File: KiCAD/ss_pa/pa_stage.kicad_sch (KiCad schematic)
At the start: 0 parts

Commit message: KiCad revC: ss_pa pa_stage initial draft + protoshield additions
ss_pa:
- First pass on pa_stage.kicad_sch: Q1/Q2 push-pull FETs, T1 output
  transformer, T2 drain-feed transformer, C3 drain snubber,
  per-FET source sense (2x 0.22R parallel per FET = 0.11R to GND)
  with Source_Sense_A/B taps, J1 coax output
- Known pending (per user): bias network, input DC-block caps,
  drain-gate feedback networks, +13.8V bulk electrolytic
- Known issues flagged in review (to be fixed on next edit):
  Q1/Q2 are IRF540N (should be IRF510 — gate capacitance mismatch),
  T2 phasing (both corresponding ends at CT → parallel winding
  instead of push-pull), no RFC between +13.8V and T2 CT
- First netlist export captured (ss_pa.net)

protoshield:
- Added capacitors C2-C3, resistors R1-R2, power symbols
  (#PWR5, #PWR22-24)

Co-Authored-By: Claude Opus 4.7 <noreply@anthropic.com>
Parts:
- added C1, C2: 1uF, symbol Device:C
- added C3: 33pF, symbol Device:C
- added J1: Conn_Coaxial_Small, symbol Connector:Conn_Coaxial_Small
- added Q1, Q2: IRF540N, Package_TO_SOT_THT:TO-220-3_Vertical, symbol Transistor_FET:IRF540N
- added R1, R2, R3, R4: 0.22R, symbol Device:R_US
- added T1, T2: Transformer_1P_1S, symbol Device:Transformer_1P_1S
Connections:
- new net: C3.2, Q2.2 (D), T1.2 (AB), T2.2 (AB)
- new net: J1.1 (In), T1.4 (SB)
- new net: C3.1, Q1.2 (D), T1.1 (AA), T2.4 (SB)
- new net +13.8V: C1.1, C2.2, T2.1 (AA), T2.3 (SA)
- new net GND: C1.2, C2.1, J1.2 (Ext), R1.2, R2.2, R3.1, R4.1, T1.3 (SA)
- new net Source_Sense_A: Q1.3 (S), R1.1, R2.1
- new net Source_Sense_B: Q2.3 (S), R3.2, R4.2
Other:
- note added: "Pin 2 and pin 3 = phase (dot)"

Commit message: KiCad revC: add xmitter:IRF510 symbol, fix Q1/Q2 metadata on pa_stage
- Added IRF510 TO-220 symbol to shared xmitter.kicad_sym (cloned IRF540N
  body graphic since pinout is identical: G=pin1, D=pin2+tab, S=pin3).
  Vishay datasheet URL, 5.6A/100V description, MPN IRF510PBF. KiCad
  standard libs don't ship an IRF510 symbol, so hosting it in the
  project's shared library.
- Updated Q1/Q2 instance-level Datasheet and Description on pa_stage
  to match (Value field was already IRF510). User will swap lib_id
  from Transistor_FET:IRF540N to xmitter:IRF510 via Change Symbol in
  KiCad to clear the lib_symbol_mismatch ERC warning.

Co-Authored-By: Claude Opus 4.7 <noreply@anthropic.com>
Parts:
- removed Q1, Q2: IRF540N, Package_TO_SOT_THT:TO-220-3_Vertical, symbol Transistor_FET:IRF540N
- added Q3, Q4: IRF510, Package_TO_SOT_THT:TO-220-3_Vertical, symbol xmitter:IRF510
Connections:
- net Source_Sense_A: now also Q3.3 (S)
- net Source_Sense_B: now also Q4.3 (S)
- net at C3.2, T1.2 (AB), T2.2 (AB): now also Q4.2 (D)
- net at C3.1, T1.1 (AA), T2.4 (SB): now also Q3.2 (D)
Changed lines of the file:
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@@
-	)
-	(symbol
-		(lib_id "Transistor_FET:IRF540N")
-		(at 158.75 109.22 0)
-		(mirror x)
-		(unit 1)
-		(body_style 1)
-		(exclude_from_sim no)
-		(in_bom yes)
-		(on_board yes)
-		(in_pos_files yes)
-		(dnp no)
-		(property "Reference" "Q2"
-			(at 165.1 107.9499 0)
-			(show_name no)
-			(do_not_autoplace no)
-			(effects
-				(font
-					(size 1.27 1.27)
-				)
-				(justify left)
-			)
-		)
-		(property "Value" "IRF540N"
-			(at 165.1 110.4899 0)
-			(show_name no)
-			(do_not_autoplace no)
-			(effects
-				(font
-					(size 1.27 1.27)
-				)
-				(justify left)
-			)
-		)
-		(property "Footprint" "Package_TO_SOT_THT:TO-220-3_Vertical"
-			(at 163.83 107.315 0)
-			(hide yes)
-			(show_name no)
-			(do_not_autoplace no)
-			(effects
-				(font
-					(size 1.27 1.27)
-					(italic yes)
-				)
-				(justify left)
-			)
-		)
-		(property "Datasheet" "http://www.irf.com/product-info/datasheets/data/irf540n.pdf"
-			(at 163.83 105.41 0)
-			(hide yes)
-			(show_name no)
-			(do_not_autoplace no)
-			(effects
-				(font
-					(size 1.27 1.27)
-				)
-				(justify left)
-			)
-		)
-		(property "Description" "33A Id, 100V Vds, HEXFET N-Channel MOSFET, TO-220"
-			(at 158.75 109.22 0)
-			(hide yes)
-			(show_name no)
-			(do_not_autoplace no)
-			(effects
-				(font
-					(size 1.27 1.27)
-				)
-			)
-		)
-		(pin "2"
-		)
-		(pin "3"
-		)
-		(pin "1"
-		)
-		(instances
-			(project "ss_pa"
-				(path "/7b9fe991-54d6-43c4-a637-0ed9ee982c42/6995ca2b-35a4-4871-8cf2-3a0067e62105"
-					(reference "Q2")
-					(unit 1)
-				)
-			)
-		)
 	)
 	(symbol
@@
 	)
 	(symbol
-		(lib_id "Transistor_FET:IRF540N")
+		(lib_id "xmitter:IRF510")
 		(at 158.75 74.93 0)
 		(unit 1)
@@
 		(dnp no)
 		(fields_autoplaced yes)
-		(property "Reference" "Q1"
+		(property "Reference" "Q3"
 			(at 165.1 73.6599 0)
 			(show_name no)
@@
 			)
 		)
-		(property "Value" "IRF540N"
+		(property "Value" "IRF510"
 			(at 165.1 76.1999 0)
 			(show_name no)
@@
 			)
 		)
-		(property "Datasheet" "http://www.irf.com/product-info/datasheets/data/irf540n.pdf"
+		(property "Datasheet" "https://www.vishay.com/docs/91015/sihf510.pdf"
 			(at 163.83 78.74 0)
 			(hide yes)
@@
 			)
 		)
-		(property "Description" "33A Id, 100V Vds, HEXFET N-Channel MOSFET, TO-220"
+		(property "Description" "5.6A Id, 100V Vds, HEXFET N-Channel MOSFET, TO-220"
 			(at 158.75 74.93 0)
 			(hide yes)
@@
 			)
 		)
-		(pin "1"
+		(property "Manufacturer" "Vishay"
+			(at 158.75 74.93 0)
+			(hide yes)
+			(show_name no)
+			(do_not_autoplace no)
+			(effects
+				(font
+					(size 1.27 1.27)
+				)
+			)
+		)
+		(property "MPN" "IRF510PBF"
+			(at 158.75 74.93 0)
+			(hide yes)
+			(show_name no)
+			(do_not_autoplace no)
+			(effects
+				(font
+					(size 1.27 1.27)
+				)
+			)
 		)
 		(pin "2"
 		)
+		(pin "1"
+		)
 		(pin "3"
 		)
@@
 			(project "ss_pa"
 				(path "/7b9fe991-54d6-43c4-a637-0ed9ee982c42/6995ca2b-35a4-4871-8cf2-3a0067e62105"
-					(reference "Q1")
+					(reference "Q3")
 					(unit 1)
 				)
@@
 					(unit 1)
 				)
+			)
+		)
+	)
+	(symbol
+		(lib_id "xmitter:IRF510")
+		(at 158.75 109.22 0)
+		(mirror x)
+		(unit 1)
+		(body_style 1)
+		(exclude_from_sim no)
+		(in_bom yes)
+		(on_board yes)
+		(in_pos_files yes)
+		(dnp no)
+		(property "Reference" "Q4"
+			(at 165.1 110.4901 0)
+			(show_name no)
+			(do_not_autoplace no)
+			(effects
+				(font
+					(size 1.27 1.27)
+				)
+				(justify left)
+			)
+		)
+		(property "Value" "IRF510"
+			(at 165.1 107.9501 0)
+			(show_name no)
+			(do_not_autoplace no)
+			(effects
+				(font
+					(size 1.27 1.27)
+				)
+				(justify left)
+			)
+		)
+		(property "Footprint" "Package_TO_SOT_THT:TO-220-3_Vertical"
+			(at 163.83 107.315 0)
+			(hide yes)
+			(show_name no)
+			(do_not_autoplace no)
+			(effects
+				(font
+					(size 1.27 1.27)
+					(italic yes)
+				)
+				(justify left)
+			)
+		)
+		(property "Datasheet" "https://www.vishay.com/docs/91015/sihf510.pdf"
+			(at 163.83 105.41 0)
+			(hide yes)
+			(show_name no)
+			(do_not_autoplace no)
+			(effects
+				(font
+					(size 1.27 1.27)
+				)
+				(justify left)
+			)
+		)
+		(property "Description" "5.6A Id, 100V Vds, HEXFET N-Channel MOSFET, TO-220"
+			(at 158.75 109.22 0)
+			(hide yes)
+			(show_name no)
+			(do_not_autoplace no)
+			(effects
+				(font
+					(size 1.27 1.27)
+				)
+			)
+		)
+		(property "Manufacturer" "Vishay"
+			(at 158.75 109.22 0)
+			(hide yes)
+			(show_name no)
+			(do_not_autoplace no)
+			(effects
+				(font
+					(size 1.27 1.27)
+				)
+			)
+		)
+		(property "MPN" "IRF510PBF"
+			(at 158.75 109.22 0)
+			(hide yes)
+			(show_name no)
+			(do_not_autoplace no)
+			(effects
+				(font
+					(size 1.27 1.27)
+				)
+			)
+		)
+		(pin "2"
+		)
+		(pin "1"
+		)
+		(pin "3"
+		)
+		(instances
+			(project "ss_pa"
+				(path "/7b9fe991-54d6-43c4-a637-0ed9ee982c42/6995ca2b-35a4-4871-8cf2-3a0067e62105"
+					(reference "Q4")
+					(unit 1)
+				)

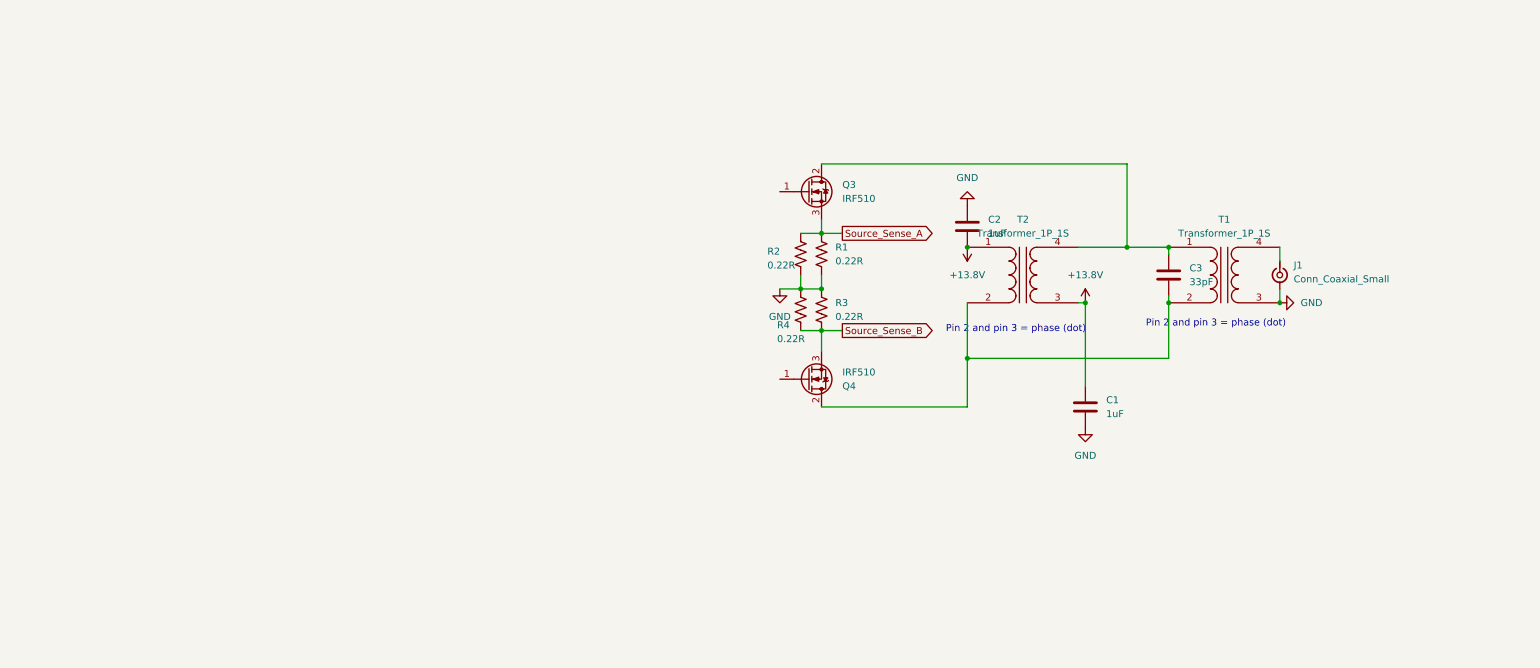
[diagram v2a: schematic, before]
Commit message: KiCad revC: ss_pa pa_stage schematic — bias network + feedback + inputs
Added since last commit:
- Per-FET bias feed: Bias_A/B → 47R series → {0.1µF decoupling, 1µH RFC}
  → gate (R7/R8, C9/C10, L3/L4)
- Per-FET drain-gate feedback: drain → 0.1µF → 220R → 1µH → gate
  (C7/C8, R5/R6, L1/L2)
- RF inputs: J3/J4 coax, each via 0.1µF DC-block (C4/C5) to gate
- +13.8V bulk electrolytic C6 (4700µF) at J2 power entry
- Instance refdesignators shifted to Q3/Q4 for the IRF510s

Netlist re-exported. All values match QRP Labs 10W Linear kit reference.
Push-pull phasing verified: T2 pin 1,4 at CT and pin 2,3 at drains gives
V(Q3) + V(Q4) = 2·V_CT (dots on pins 2,3 per KiCad library convention).

Pending: Bias_A/B and Source_Sense_A/B still need umbilical connector.
No RFC between +13.8V and T2 CT — matches kit (L201 is at supply entry
on kit schematic, not between +12V bus and T203 CT).

Co-Authored-By: Claude Opus 4.7 <noreply@anthropic.com>
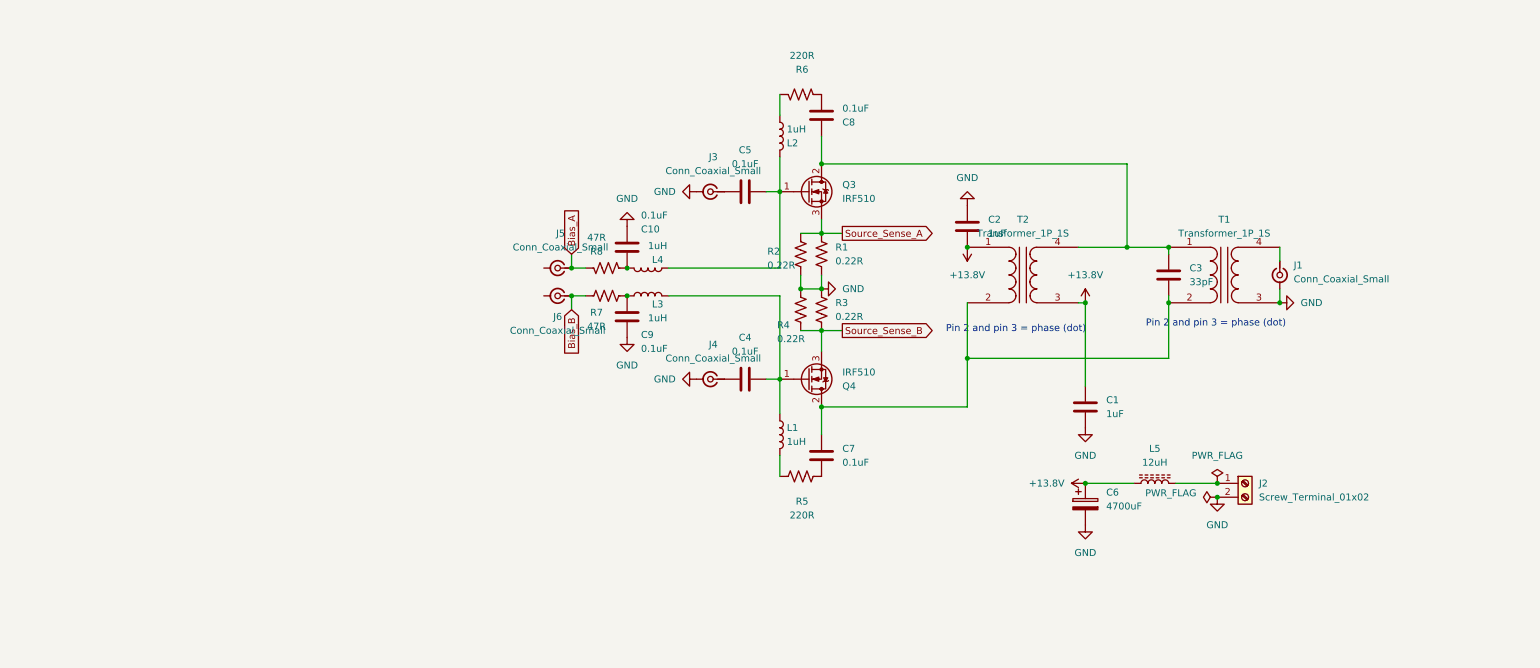
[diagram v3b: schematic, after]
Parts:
- added C10, C4, C5, C7, C8, C9: 0.1uF, symbol Device:C
- added C6: 4700uF, symbol Device:C_Polarized
- added J2: Screw_Terminal_01x02, symbol Connector:Screw_Terminal_01x02
- added J3, J4, J5, J6: Conn_Coaxial_Small, symbol Connector:Conn_Coaxial_Small
- added L1, L2, L3, L4: 1uH, symbol Device:L
- added L5: 12uH, symbol Device:L_Ferrite
- added R5, R6: 220R, symbol Device:R_US
- added R7, R8: 47R, symbol Device:R_US
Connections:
- net +13.8V: now also C6.1, L5.1
- net GND: now also C10.2, C6.2, C9.2, J2.2 (Pin_2), J3.2 (Ext), J4.2 (Ext)
- net at Q3.1 (G): now also C5.2, L2.1, L4.2
- net at C3.1, Q3.2 (D), T1.1 (AA)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: now also C8.2
- net at C3.2, Q4.2 (D), T1.2 (AB)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: now also C7.2
- net at Q4.1 (G): now also C4.2, L1.1, L3.2
- new net: L2.2, R6.1
- new net: C8.1, R6.2
- new net: J2.1 (Pin_1), L5.2
- new net: C7.1, R5.2
- new net: L1.2, R5.1
- new net: C5.1, J3.1 (In)
- new net: C10.1, L4.1, R8.2
- new net: C9.1, L3.1, R7.2
- new net: C4.1, J4.1 (In)
- new net Bias_A: J5.1 (In), R8.1
- new net Bias_B: J6.1 (In), R7.1

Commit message: KiCad revC: ss_pa pa_stage schematic refinements
Continued work on pa_stage.kicad_sch after the review pass.

Co-Authored-By: Claude Opus 4.7 <noreply@anthropic.com>
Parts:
- removed J5, J6: Conn_Coaxial_Small, symbol Connector:Conn_Coaxial_Small
- added J7: 8P8C_Shielded, xmitter:Amphenol_RJE1D-188_Horizontal_Shielded, symbol Connector:8P8C_Shielded
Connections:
- net GND: now also J7.2, J7.5, J7.6, J7.SH
- net Source_Sense_A: now also J7.1
- net Source_Sense_B: now also J7.4
- new net Bias_A_Raw: J7.7
- new net Bias_B_Raw: J7.8
- new net FAULT: J7.3

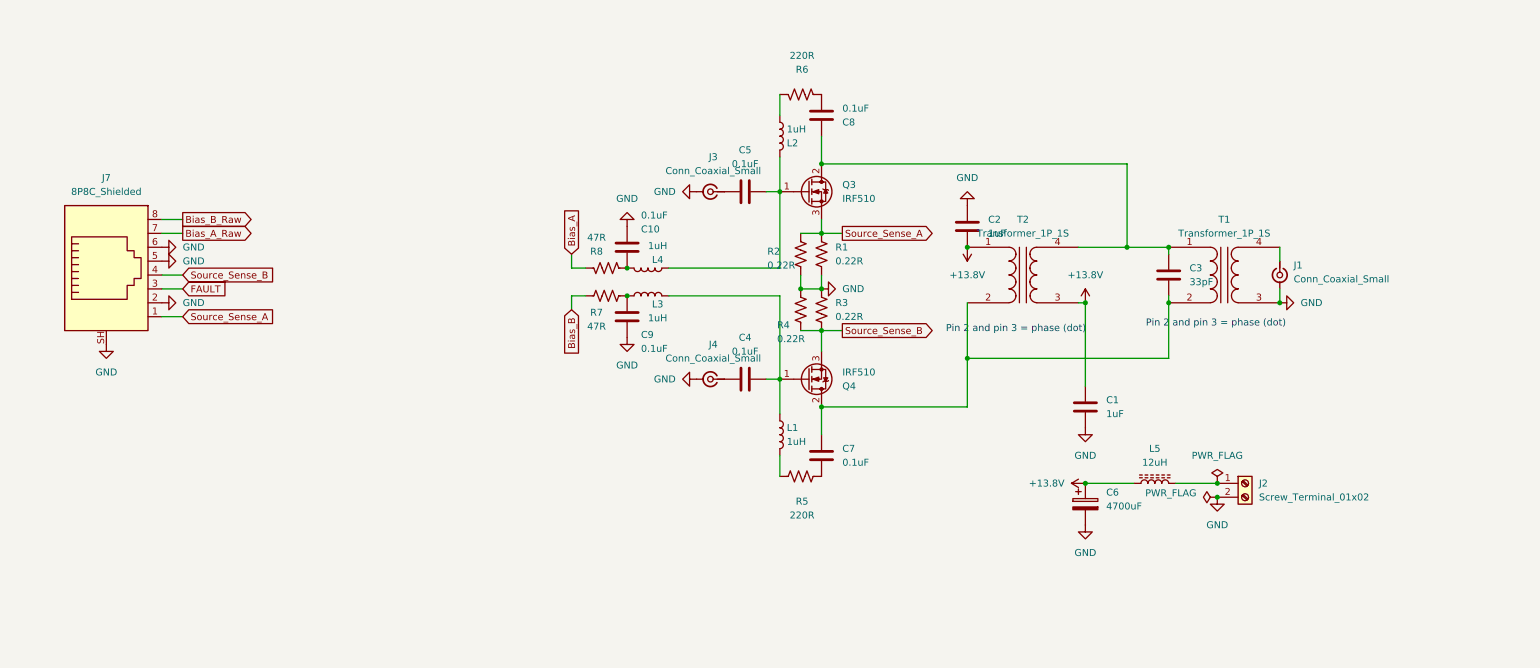
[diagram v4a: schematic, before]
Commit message: KiCad revC: ss_pa fault_shutdown populated + CD74HC4066 symbol + doc
Fault_shutdown sheet implemented with the self-latching V_REF scheme:
- LM393 (U1) powered from +3.3V (via RJ45 pin 6 from analog board)
- V_REF divider (R11=100K, R10=10K) powered from FAULT_N bus, giving
  intrinsic self-latching when fault asserts (no flip-flop needed) —
  normal V_REF ≈ 288 mV, fault V_REF = 0
- Pullup R9 (4.7K) on FAULT_N to +3.3V, wire-OR of both LM393 outputs
- FAULT_N is active-low (user renamed from FAULT after wire-OR polarity
  analysis — open-collector wire-OR of multiple fault sources requires
  LOW = fault for proper OR behavior)
- Startup cap C12 (1uF) + D1 (1N4148, cathode to V_REF) auto-resets
  the latch at power-on without needing button press
- CD74HC4066 (U2) in series with Bias_A/Bias_B lines — control pins
  tied to FAULT_N (HIGH=closed, LOW=open). Series-pass approach
  (not shunt-to-GND) avoids loading the MCP4728 DAC during a latched
  fault
- Reset: J5 screw terminal for external pushbutton; shorts +3.3V to
  V_REF momentarily to break the latch
- Noise filtering: C11 (0.01uF) on FAULT_N bus; C14/C15 (0.1uF each)
  bypass caps for U1 and U2
- RJ45 J7 (Amphenol RJE1D-188 shielded 8P8C) per T568B pair plan;
  shield grounded on PA-board end only

PA stage additions since last commit:
- L5 (12 uH on FT50-43, 5-6 turns) — supply input RFC between J2
  power entry and the +13.8V bus (L201-equivalent per QRP Labs kit)
- Fixed earlier wiring bugs flagged in review: U1 pin 6 moved from
  Source_Sense_A to Source_Sense_B so comparator B monitors Q4; C13
  replaced by C15 wired correctly as U2 bypass cap

Library:
- Added CD74HC4066 symbol (PDIP-14) to xmitter.kicad_sym with
  TI-style pinout; footprint = Package_DIP:DIP-14_W7.62mm

Documentation:
- Documentation/ss_pa.md rewritten to reflect as-built design:
  updated RJ45 pin assignment (pin 6 = +3.3V, pin 3 = FAULT_N),
  added L5 to supply decoupling, full rewrite of fault_shutdown
  section with the self-latchi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
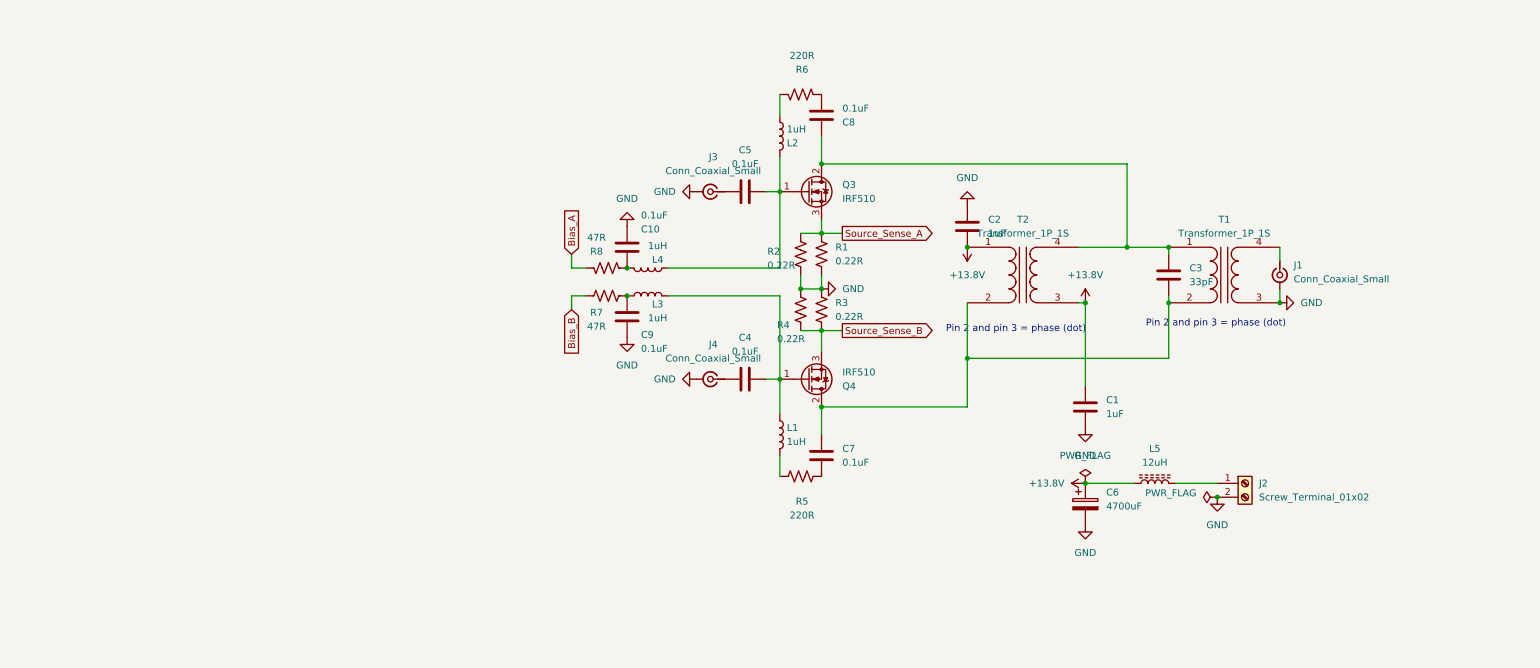
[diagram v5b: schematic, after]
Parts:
- removed J7: 8P8C_Shielded, xmitter:Amphenol_RJE1D-188_Horizontal_Shielded, symbol Connector:8P8C_Shielded
